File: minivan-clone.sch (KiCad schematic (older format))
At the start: 21 parts, among them CON101 HRO-TYPE-C-31-M-12, SW101 SW_PUSH, U101 ATMEGA32U2, X101 XTAL_GND

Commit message: fixed pour
fixed pour
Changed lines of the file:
@@
 Text Label 2750 4500 0    50   ~ 0
 PD6
-Text Label 2750 5000 0    50   ~ 0
+Text Label 2750 4600 0    50   ~ 0
 PB0
 Text Label 2750 5600 0    50   ~ 0
@@
 Text Label 2750 5800 0    50   ~ 0
 PB6
-Text Label 2750 5900 0    50   ~ 0
-PC6
 Text Label 2750 6000 0    50   ~ 0
-PC5
+PB7
 Text Label 2750 6100 0    50   ~ 0
 PC4
 Text Label 2750 4700 0    50   ~ 0
 PB1
-Text Label 2750 4600 0    50   ~ 0
+Text Label 2750 4800 0    50   ~ 0
 PB3
 Text Label 2750 5400 0    50   ~ 0
@@
 Wire Wire Line
 	2650 5400 2750 5400
-Text Label 2750 4800 0    50   ~ 0
+Text Label 2750 5000 0    50   ~ 0
 PB2
+Text Label 2750 5900 0    50   ~ 0
+PC6
 $EndSCHEMATC

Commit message: started mirroring keyboard layout
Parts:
- CON101: symbol minivan-clone-rescue:HRO-TYPE-C-31-M-12-Type-C-minivan-clone-rescue -> minivan-clone-rescue:HRO-TYPE-C-31-M-12-Type-C-minivan-clone-rescue-minivan-clone-rescue
- D202: symbol Power_Protection:PRTR5V0U2X -> minivan-clone-rescue:PRTR5V0U2X-Power_Protection
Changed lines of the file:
@@
 EESchema Schematic File Version 4
 LIBS:minivan-clone-cache
-EELAYER 29 0
+EELAYER 30 0
 EELAYER END
 $Descr A4 11693 8268
@@
 	1950 2750 1950 2650
 $Comp
-L minivan-clone-rescue:HRO-TYPE-C-31-M-12-Type-C-minivan-clone-rescue CON101
+L minivan-clone-rescue:HRO-TYPE-C-31-M-12-Type-C-minivan-clone-rescue-minivan-clone-rescue CON101
 U 1 1 5D1BD550
 P 1850 2100
@@
 	7350 5900 8150 5900
 $Comp
-L power:GND #PWR0101
+L minivan-clone-rescue:GND-power #PWR0101
 U 1 1 5D783424
 P 9900 1150
@@
 $EndComp
 $Comp
-L power:GND #PWR0103
+L minivan-clone-rescue:GND-power #PWR0103
 U 1 1 5D783D84
 P 11050 2000
@@
 $EndComp
 $Comp
-L power:GND #PWR0104
+L minivan-clone-rescue:GND-power #PWR0104
 U 1 1 5D7843A4
 P 10300 2350
@@
 $EndComp
 $Comp
-L power:GND #PWR0105
+L minivan-clone-rescue:GND-power #PWR0105
 U 1 1 5D784B88
 P 5850 2750
@@
 $EndComp
 $Comp
-L power:GND #PWR0106
+L minivan-clone-rescue:GND-power #PWR0106
 U 1 1 5D784E14
 P 6850 1250
@@
 $EndComp
 $Comp
-L power:GND #PWR0107
+L minivan-clone-rescue:GND-power #PWR0107
 U 1 1 5D785521
 P 5350 1800
@@
 $EndComp
 $Comp
-L power:GND #PWR0108
+L minivan-clone-rescue:GND-power #PWR0108
 U 1 1 5D7857C7
 P 4750 1800
@@
 Connection ~ 4750 1800
 $Comp
-L power:GND #PWR0109
+L minivan-clone-rescue:GND-power #PWR0109
 U 1 1 5D785DFD
 P 1950 1550
@@
 $EndComp
 $Comp
-L power:GND #PWR0110
+L minivan-clone-rescue:GND-power #PWR0110
 U 1 1 5D7865E1
 P 1950 2750
@@
 Connection ~ 1950 2750
 $Comp
-L power:GND #PWR0111
+L minivan-clone-rescue:GND-power #PWR0111
 U 1 1 5D78689D
 P 2500 3100
@@
 	2500 3100 2700 3100
 $Comp
-L power:GND #PWR0112
+L minivan-clone-rescue:GND-power #PWR0112
 U 1 1 5D786B67
 P 8150 5900
@@
 	8150 5900 8500 5900
 $Comp
-L Power_Protection:PRTR5V0U2X D202
+L minivan-clone-rescue:PRTR5V0U2X-Power_Protection D202
 U 1 1 5D787265
 P 5250 4000
@@
 $EndComp
 $Comp
-L power:GND #PWR0113
+L minivan-clone-rescue:GND-power #PWR0113
 U 1 1 5D7884C0
 P 5250 4500
@@
 pre_D+
 $Comp
-L power:+5V #PWR0102
+L minivan-clone-rescue:+5V-power #PWR0102
 U 1 1 5D78AA14
 P 5250 3500
@@
 $EndComp
 $Comp
-L power:+5V #PWR0114
+L minivan-clone-rescue:+5V-power #PWR0114
 U 1 1 5D78B5BE
 P 3000 1650
@@
 $EndComp
 $Comp
-L power:+5V #PWR0115
+L minivan-clone-rescue:+5V-power #PWR0115
 U 1 1 5D78C361
 P 6850 1350
@@
 $EndComp
 $Comp
-L power:+5V #PWR0116
+L minivan-clone-rescue:+5V-power #PWR0116
 U 1 1 5D78C75A
 P 9000 1050
@@
 Connection ~ 9000 1050
 $Comp
-L power:GND #PWR0117
+L minivan-clone-rescue:GND-power #PWR0117
 U 1 1 5D792811
 P 9000 1450
@@
 $EndComp
 $Comp
-L power:+5V #PWR0118
+L minivan-clone-rescue:+5V-power #PWR0118
 U 1 1 5D792F03
 P 10300 1300
@@
 $EndComp
 $Comp
-L power:+5V #PWR0119
+L minivan-clone-rescue:+5V-power #PWR0119
 U 1 1 5D793283
 P 8150 5500

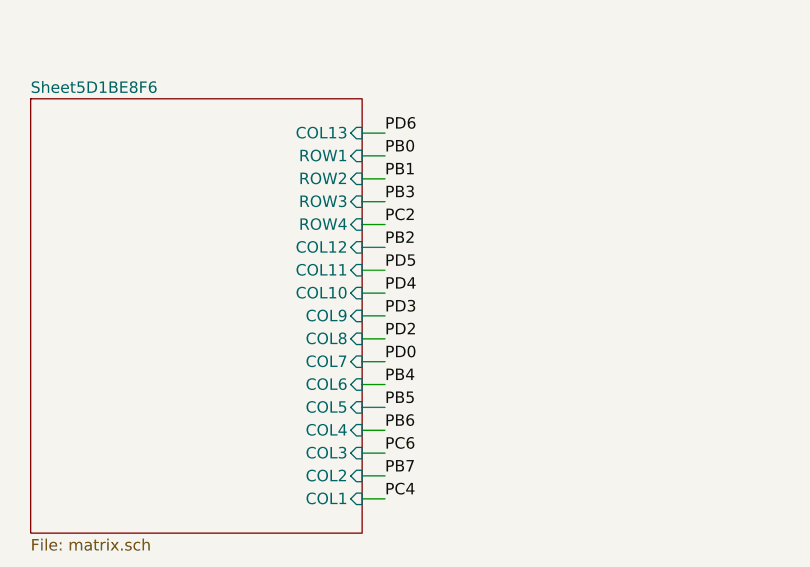
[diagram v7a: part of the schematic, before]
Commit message: more tracks for leftmost cols
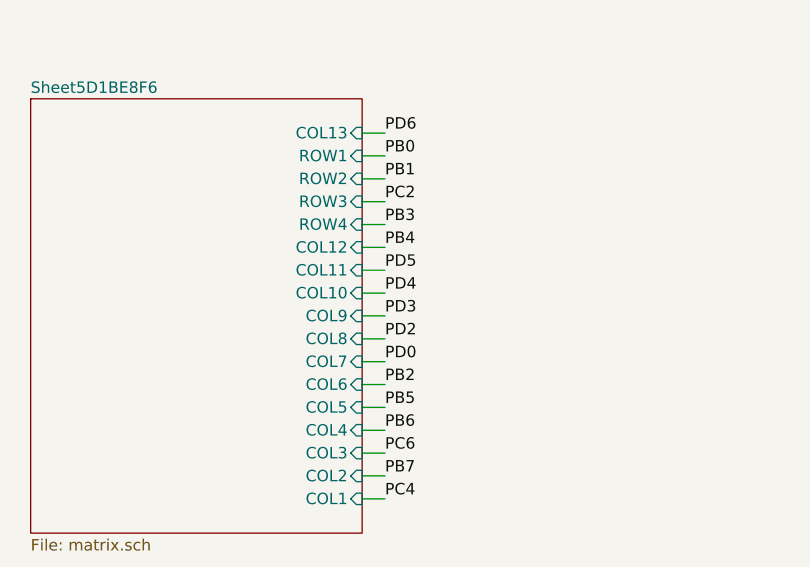
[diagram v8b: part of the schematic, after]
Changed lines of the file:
@@
 	1    0    0    -1
 $EndComp
-Text Label 2750 4900 0    50   ~ 0
+Text Label 2750 4800 0    50   ~ 0
 PC2
 Text Label 2750 5500 0    50   ~ 0
@@
 Text Label 2750 4600 0    50   ~ 0
 PB0
-Text Label 2750 5600 0    50   ~ 0
-PB4
 Text Label 2750 5700 0    50   ~ 0
 PB5
@@
 Text Label 2750 4700 0    50   ~ 0
 PB1
-Text Label 2750 4800 0    50   ~ 0
+Text Label 2750 4900 0    50   ~ 0
 PB3
 Text Label 2750 5400 0    50   ~ 0
@@
 Wire Wire Line
 	2650 5400 2750 5400
-Text Label 2750 5000 0    50   ~ 0
+Text Label 2750 5600 0    50   ~ 0
 PB2
 Text Label 2750 5900 0    50   ~ 0
 PC6
+Text Label 2750 5000 0    50   ~ 0
+PB4
 $EndSCHEMATC
